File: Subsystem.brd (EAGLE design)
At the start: 100 x 80 mm, 20 parts

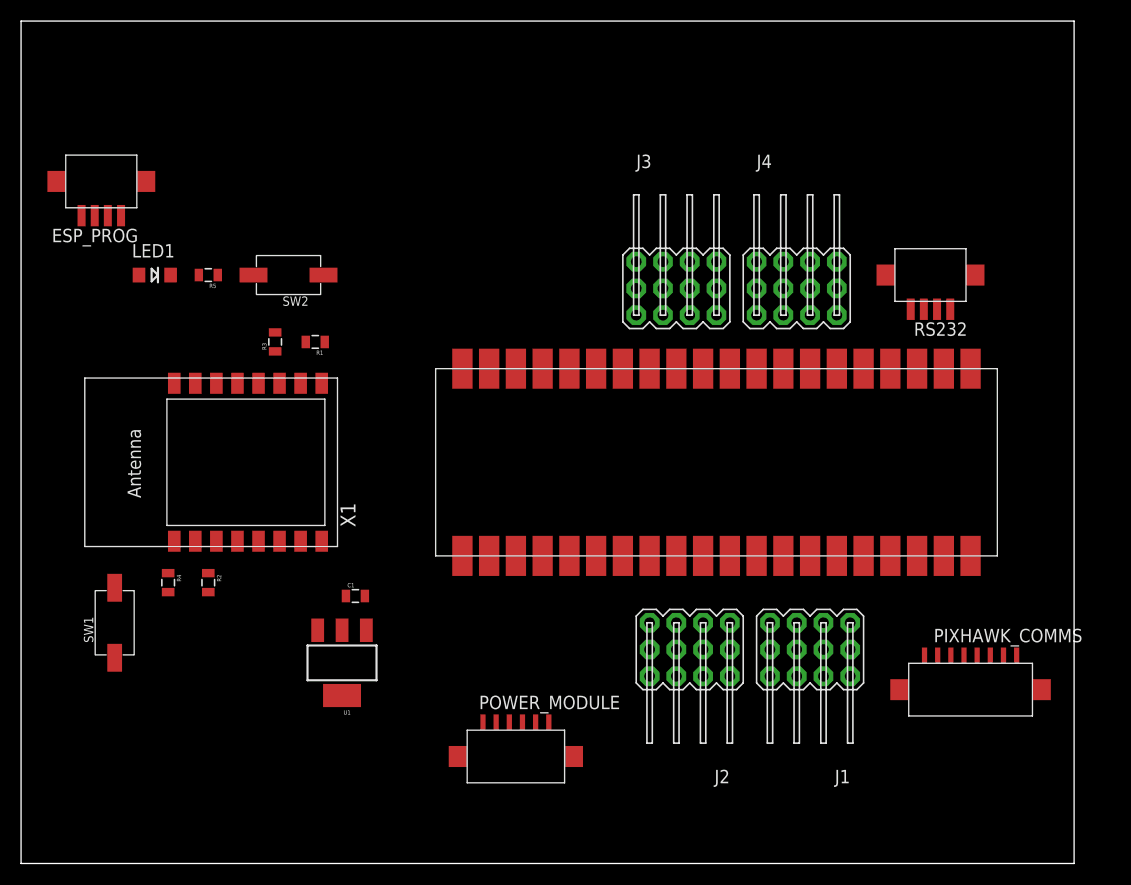
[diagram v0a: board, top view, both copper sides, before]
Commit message: Schematic V2\n Check for errors
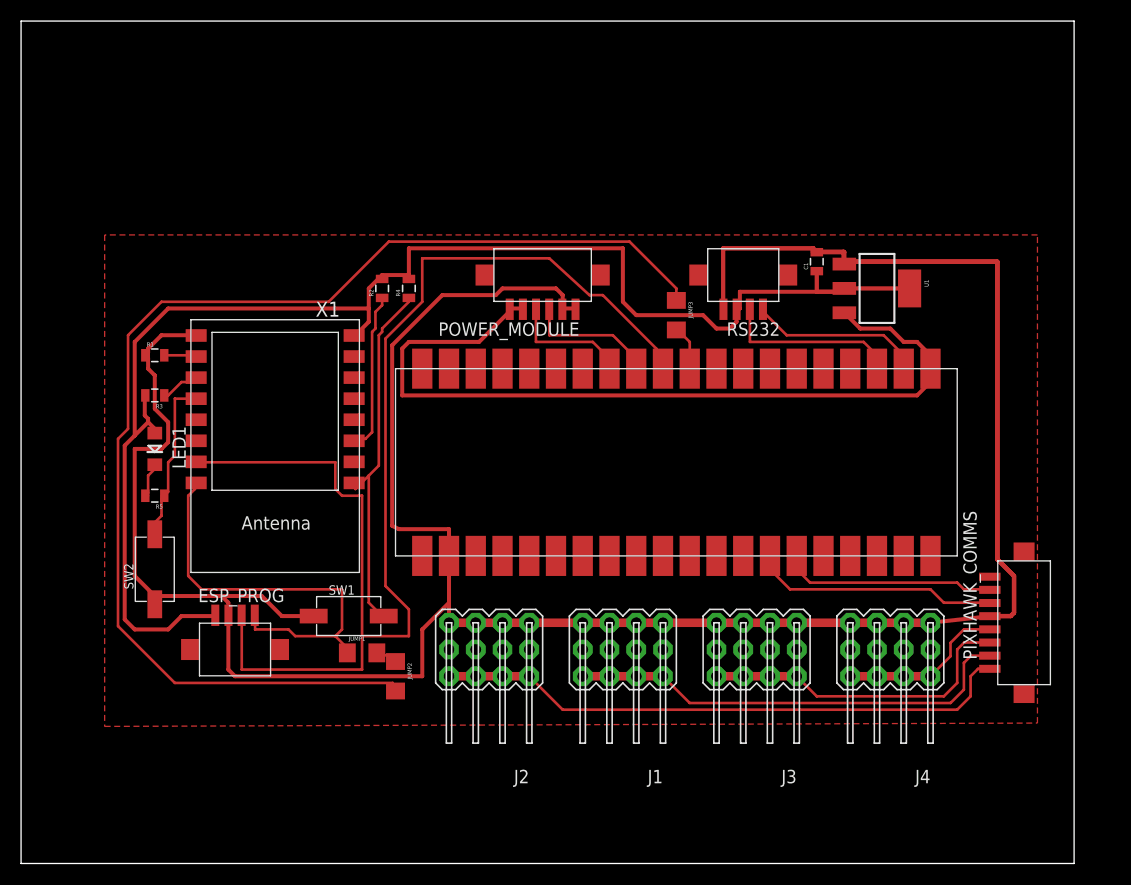
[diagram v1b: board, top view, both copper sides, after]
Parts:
- added JUMP1, JUMP2, JUMP3: 0, Brendan:1206
- moved U1 62.0 mm to (81.3, 54.6), turned to 270 degrees
- moved C1 54.1 mm to (75.6, 57.1), turned to 90 degrees
- moved ESP_PROG 46.2 mm to (20.3, 20.3), turned to 0 degrees
- moved POWER_MODULE 45.8 mm to (49.5, 55.9), turned to 180 degrees
- moved R4 36.1 mm to (36.8, 54.6), turned to 90 degrees
- moved J4 35.4 mm to (82.5, 20.3), turned to 180 degrees
- moved J3 35.1 mm to (69.8, 20.3), turned to 180 degrees
- moved R2 32.5 mm to (34.3, 54.6), turned to 90 degrees
- moved SW2 30.7 mm to (12.7, 27.9), turned to 90 degrees
- moved SW1 22.2 mm to (31.1, 23.5), turned to 0 degrees
- moved R5 21.6 mm to (12.7, 34.9)
- moved J2 19.0 mm to (44.5, 20.3)
- moved J1 17.8 mm to (57.1, 20.3)
- moved RS232 17.8 mm to (68.6, 55.9)
- moved LED1 16.5 mm to (12.7, 39.4), turned to 270 degrees
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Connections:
- net 3.3V: now also ESP_PROG.P$1, RS232.P$3, U1.4; no longer ESP_PROG.P$4, RS232.P$4
- net GND: now also ESP_PROG.P$2, PIXHAWK_COMMS.P$5, RS232.P$4, U1.1; no longer ESP_PROG.P$1, PIXHAWK_COMMS.P$1, RS232.P$1, U1.4
- net MCUR: now also POWER_MODULE.P$3, U$1.P$12; no longer POWER_MODULE.P$4, U$1.P$8
- net MVOL: now also POWER_MODULE.P$4, U$1.P$13; no longer POWER_MODULE.P$3, U$1.P$9
- net PWM1: now also PIXHAWK_COMMS.P$4; no longer PIXHAWK_COMMS.P$2
- net PWM3: now also PIXHAWK_COMMS.P$1; no longer PIXHAWK_COMMS.P$4
- net PWM4: now also PIXHAWK_COMMS.P$2; no longer PIXHAWK_COMMS.P$5
- net RX2: now also ESP_PROG.P$4, JUMP1.1, JUMP1.2, JUMP2.1, JUMP2.2, JUMP3.1, JUMP3.2; no longer ESP_PROG.P$2
- net RX3: now also RS232.P$1; no longer RS232.P$3
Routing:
- net GND: track 0.00 -> 270.9 mm
- net RX2: track 0.00 -> 163.6 mm
- net 3.3V: track 0.00 -> 139.7 mm
- net TX2: track 0.00 -> 122.2 mm
- net 5V: track 0.00 -> 80.8 mm
- net PWM3: track 0.00 -> 55.4 mm
- net N$1: track 0.00 -> 50.3 mm
- net PWM4: track 0.00 -> 43.1 mm
- net RESET: track 0.00 -> 34.9 mm
- net PWM2: track 0.00 -> 30.7 mm
- net RX1: track 0.00 -> 23.5 mm
- net TX1: track 0.00 -> 20.4 mm
- net TX3: track 0.00 -> 17.0 mm
- net RX3: track 0.00 -> 16.6 mm
- net GPIO0: track 0.00 -> 16.0 mm
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- added copper zone on layer 1, net GND
